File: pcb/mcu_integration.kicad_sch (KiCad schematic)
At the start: 26 parts, among them J1 Micro_SD_Card, J3 Conn_01x06, U1 STM32F103RBTx, Y1 ECS-80-18-5PX-GM-TR

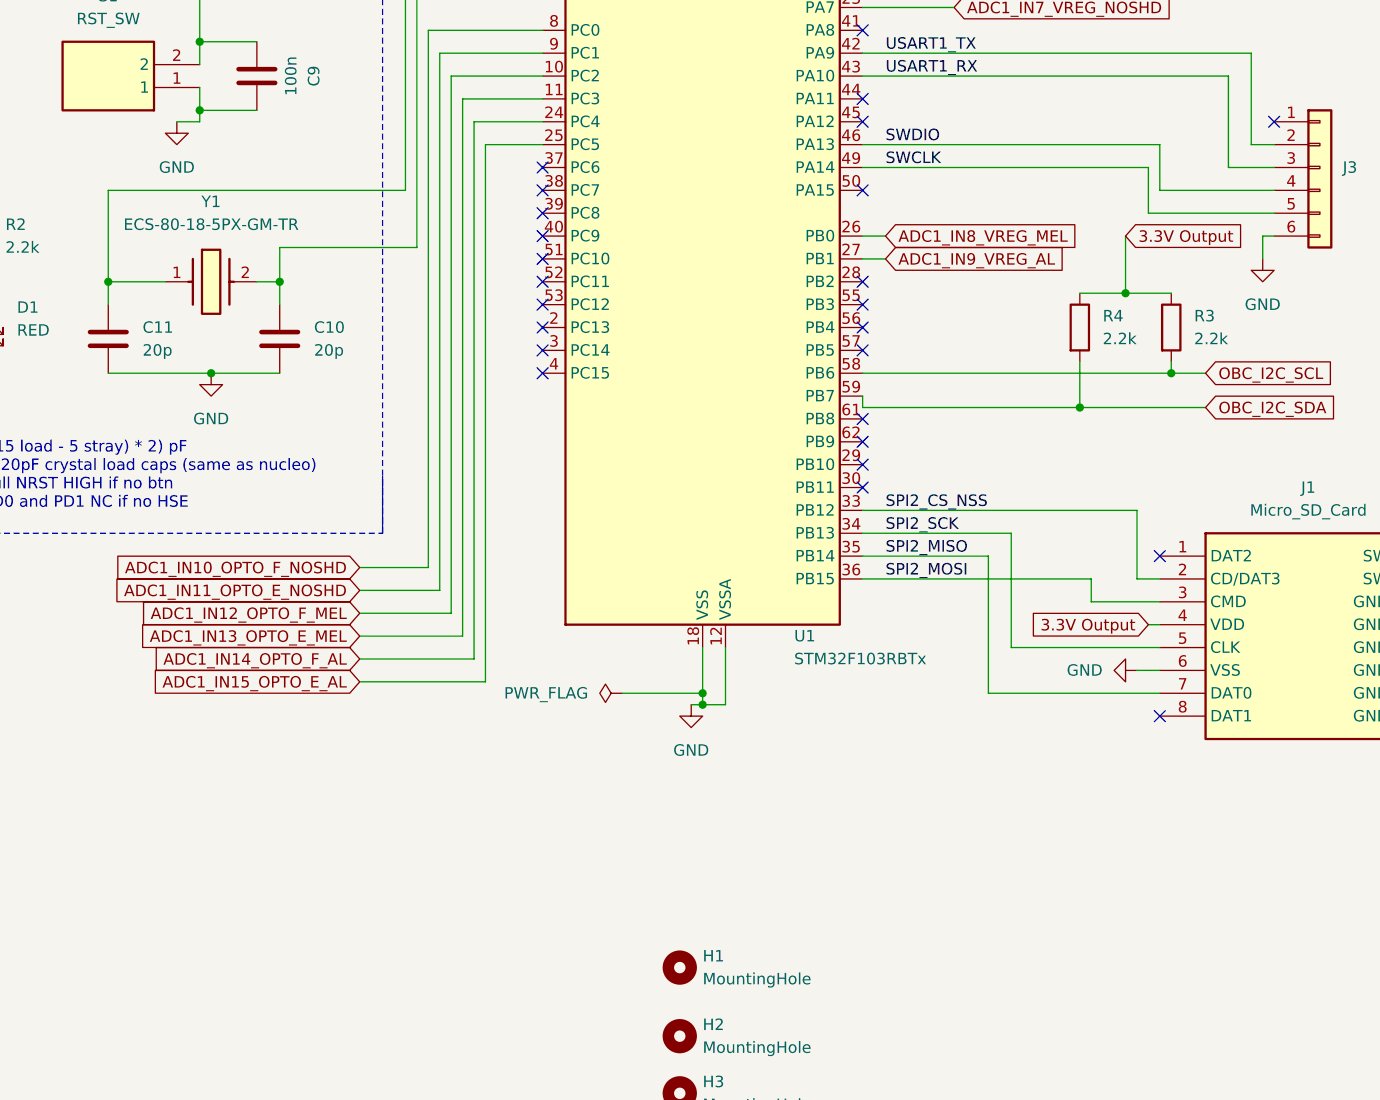
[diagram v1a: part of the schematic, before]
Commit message: Wire touchup, initial changes (#12)
* Implemented mosfet, decoupling

Please review functionality

* wire placement, inital revisions

made it more PCB ready with spacing and such
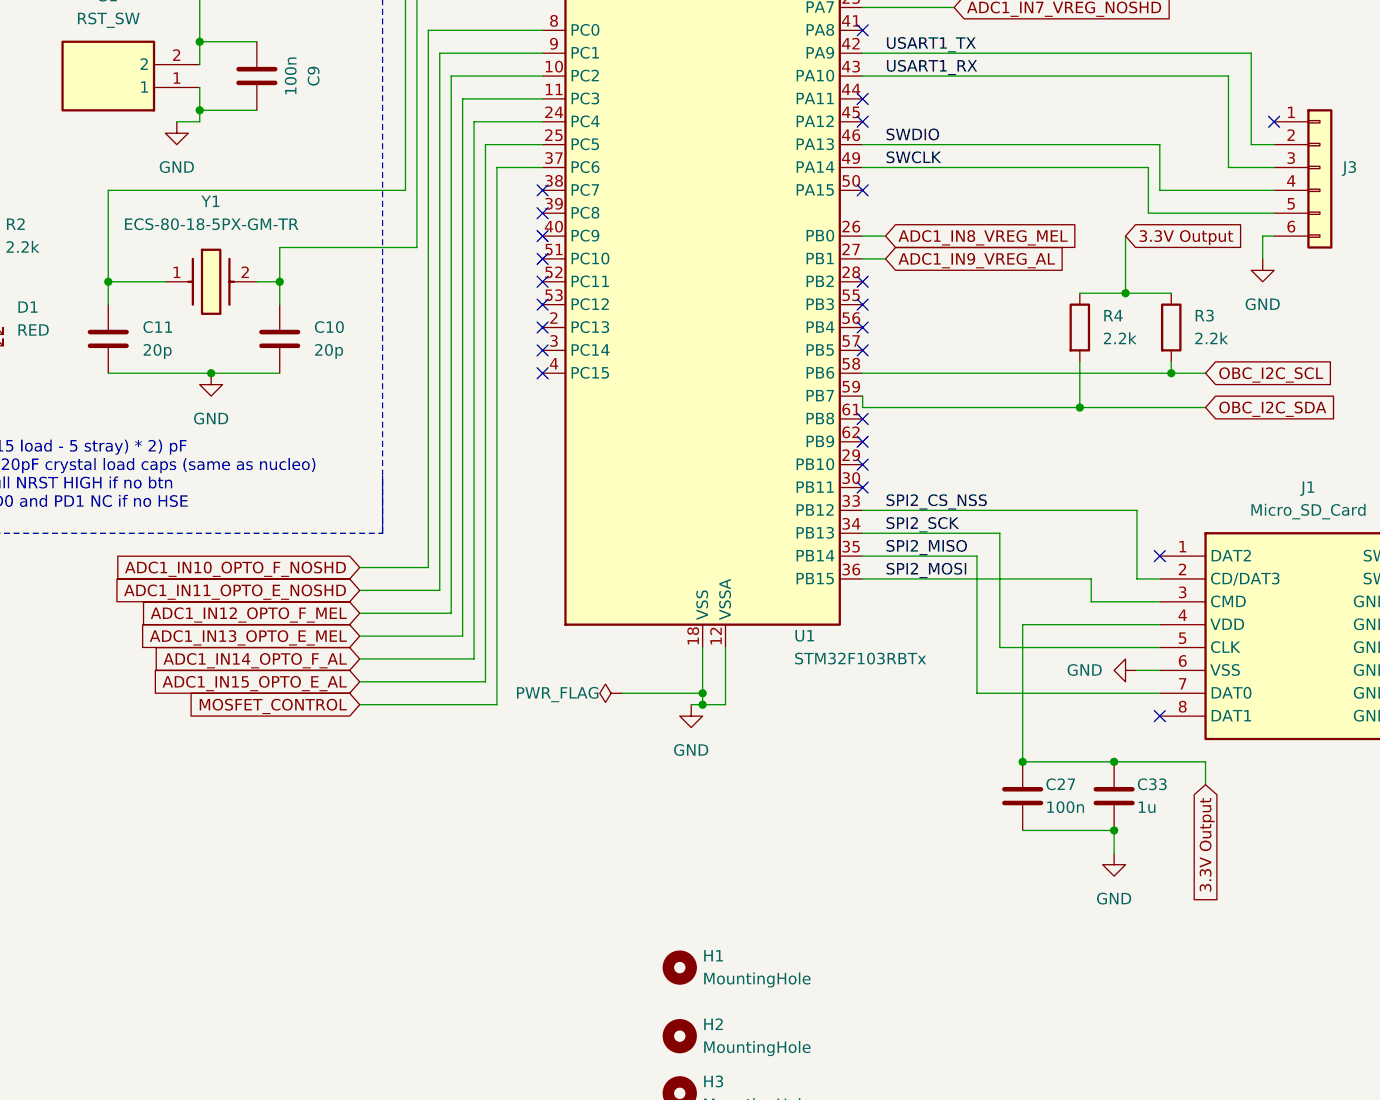
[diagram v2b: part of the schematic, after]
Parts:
- added C27: 100n, Capacitor_SMD:C_0402_1005Metric, symbol Device:C
- added C33: 1u, Capacitor_SMD:C_0402_1005Metric, symbol Device:C
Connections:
- net 3.3V Output: now also C27.1, C33.1
- net GND: now also C27.2, C33.2
- net MOSFET_CONTROL: now reaches U1.37 (PC6)
- no-connect marks 28 -> 27
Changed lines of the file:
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@@
   (junction (at 33.02 85.09) (diameter 0) (color 0 0 0 0)
   )
+  (junction (at 144.78 146.05) (diameter 0) (color 0 0 0 0)
+  )
   (junction (at 93.98 30.48) (diameter 0) (color 0 0 0 0)
   )
@@
   (junction (at 52.07 24.13) (diameter 0) (color 0 0 0 0)
   )
+  (junction (at 134.62 138.43) (diameter 0) (color 0 0 0 0)
+  )
   (junction (at 118.11 20.32) (diameter 0) (color 0 0 0 0)
   )
@@
   )
   (junction (at 63.5 24.13) (diameter 0) (color 0 0 0 0)
+  )
+  (junction (at 144.78 138.43) (diameter 0) (color 0 0 0 0)
   )
   (no_connect (at 81.28 90.17))
@@
   (no_connect (at 116.84 100.33))
   (no_connect (at 116.84 64.77))
-  (no_connect (at 81.28 72.39))
   (no_connect (at 182.88 118.11))
   (no_connect (at 116.84 74.93))
@@
   (no_connect (at 182.88 115.57))
   (no_connect (at 81.28 52.07))
+  (wire (pts (xy 134.62 146.05) (xy 144.78 146.05))
+    (stroke (width 0) (type default))
+  )
   (wire (pts (xy 39.37 24.13) (xy 52.07 24.13))
     (stroke (width 0) (type default))
@@
     (stroke (width 0) (type default))
   )
-  (wire (pts (xy 133.35 113.03) (xy 116.84 113.03))
+  (wire (pts (xy 132.08 113.03) (xy 116.84 113.03))
     (stroke (width 0) (type default))
   )
   (wire (pts (xy 66.04 46.99) (xy 81.28 46.99))
+    (stroke (width 0) (type default))
+  )
+  (wire (pts (xy 154.94 140.97) (xy 154.94 138.43))
     (stroke (width 0) (type default))
   )
@@
     (stroke (width 0) (type default))
   )
+  (wire (pts (xy 144.78 148.59) (xy 144.78 146.05))
+    (stroke (width 0) (type default))
+  )
+  (wire (pts (xy 60.96 132.08) (xy 76.2 132.08))
+    (stroke (width 0) (type default))
+  )
   (wire (pts (xy 106.68 21.59) (xy 106.68 31.75))
     (stroke (width 0) (type default))
@@
     (stroke (width 0) (type default))
   )
-  (wire (pts (xy 130.81 115.57) (xy 130.81 130.81))
+  (wire (pts (xy 129.54 115.57) (xy 129.54 130.81))
     (stroke (width 0) (type default))
   )
@@
     (stroke (width 0) (type default))
   )
-  (wire (pts (xy 149.86 125.73) (xy 133.35 125.73))
+  (wire (pts (xy 149.86 125.73) (xy 132.08 125.73))
     (stroke (width 0) (type default))
   )
@@
     (stroke (width 0) (type default))
   )
+  (wire (pts (xy 154.94 138.43) (xy 144.78 138.43))
+    (stroke (width 0) (type default))
+  )
   (wire (pts (xy 116.84 110.49) (xy 147.32 110.49))
     (stroke (width 0) (type default))
@@
   )
   (wire (pts (xy 146.05 80.01) (xy 146.05 86.36))
+    (stroke (width 0) (type default))
+  )
+  (wire (pts (xy 134.62 123.19) (xy 149.86 123.19))
     (stroke (width 0) (type default))
   )
@@
     (stroke (width 0) (type default))
   )
-  (wire (pts (xy 148.59 123.19) (xy 149.86 123.19))
-    (stroke (width 0) (type default))
-  )
   (wire (pts (xy 76.2 40.64) (xy 76.2 41.91))
     (stroke (width 0) (type default))
@@
     (stroke (width 0) (type default))
   )
+  (wire (pts (xy 129.54 130.81) (xy 149.86 130.81))
+    (stroke (width 0) (type default))
+  )
   (wire (pts (xy 52.07 81.28) (xy 67.31 81.28))
     (stroke (width 0) (type default))
   )
-  (wire (pts (xy 133.35 125.73) (xy 133.35 113.03))
+  (wire (pts (xy 132.08 125.73) (xy 132.08 113.03))
     (stroke (width 0) (type default))
   )
@@
     (stroke (width 0) (type dash))
   )
+  (wire (pts (xy 134.62 123.19) (xy 134.62 138.43))
+    (stroke (width 0) (type default))
+  )
   (wire (pts (xy 116.84 59.69) (xy 160.02 59.69))
     (stroke (width 0) (type default))
   )
-  (wire (pts (xy 130.81 130.81) (xy 149.86 130.81))
-    (stroke (width 0) (type default))
-  )
   (wire (pts (xy 147.32 110.49) (xy 147.32 118.11))
     (stroke (width 0) (type default))
   )
+  (wire (pts (xy 76.2 72.39) (xy 76.2 132.08))
+    (stroke (width 0) (type default))
+  )
   (wire (pts (xy 162.56 74.93) (xy 149.86 74.93))
     (stroke (width 0) (type default))
@@
     (stroke (width 0) (type default))
   )
+  (wire (pts (xy 134.62 138.43) (xy 144.78 138.43))
+    (stroke (width 0) (type default))
+  )
+  (wire (pts (xy 81.28 72.39) (xy 76.2 72.39))
+    (stroke (width 0) (type default))
+  )
   (wire (pts (xy 149.86 74.93) (xy 149.86 69.85))
     (stroke (width 0) (type default))
@@
     (stroke (width 0) (type default))
   )
-  (wire (pts (xy 116.84 115.57) (xy 130.81 115.57))
+  (wire (pts (xy 116.84 115.57) (xy 129.54 115.57))
     (stroke (width 0) (type default))
   )
@@
   (label "SPI2_SCK" (at 119.38 113.03 0) (fields_autoplaced)
     (effects (font (size 1.27 1.27)) (justify left bottom))
+  )
+  (global_label "3.3V Output" (shape input) (at 154.94 140.97 270) (fields_autoplaced)
+    (effects (font (size 1.27 1.27)) (justify right))
+    (property "Intersheetrefs" "${INTERSHEET_REFS}" (at 154.94 155.2641 90)
+      (effects (font (size 1.27 1.27)) (justify right) hide)
+    )
   )
   (global_label "ADC1_IN6_VREF_AL" (shape input) (at 127 52.07 0) (fields_autoplaced)
@@
     )
   )
+  (global_label "MOSFET_CONTROL" (shape input) (at 60.96 132.08 180) (fields_autoplaced)
+    (effects (font (size 1.27 1.27)) (justify right))
+    (property "Intersheetrefs" "${INTERSHEET_REFS}" (at 41.2834 132.08 0)
+      (effects (font (size 1.27 1.27)) (justify right) hide)
+    )
+  )
   (global_label "ADC1_IN2_OPAMP_MEL" (shape input) (at 127 41.91 0) (fields_autoplaced)
     (effects (font (size 1.27 1.27)) (justify left))
@@
     (property "Intersheetrefs" "${INTERSHEET_REFS}" (at 149.0956 49.53 0)
       (effects (font (size 1.27 1.27)) (justify left) hide)
-    )
-  )
-  (global_label "3.3V Output" (shape input) (at 148.59 123.19 180) (fields_autoplaced)
-    (effects (font (size 1.27 1.27)) (justify right))
-    (property "Intersheetrefs" "${INTERSHEET_REFS}" (at 134.2959 123.19 0)
-      (effects (font (size 1.27 1.27)) (justify right) hide)
     )
   )
@@
     )
   )
+  (symbol (lib_id "power:GND") (at 144.78 148.59 0) (unit 1)
+    (in_bom yes) (on_board yes) (dnp no) (fields_autoplaced)
+    (property "Reference" "#PWR05" (at 144.78 154.94 0)
+      (effects (font (size 1.27 1.27)) hide)
+    )
+    (property "Value" "GND" (at 144.78 153.67 0)
+      (effects (font (size 1.27 1.27)))
+    )
+    (property "Footprint" "" (at 144.78 148.59 0)
+      (effects (font (size 1.27 1.27)) hide)
+    )
+    (property "Datasheet" "" (at 144.78 148.59 0)
+      (effects (font (size 1.27 1.27)) hide)
+    )
+    (pin "1")
+    (instances
+      (project "mcu_integration"
+        (path "/c0210bc3-f67f-47d8-a34e-f002a728adb2"
+          (reference "#PWR05") (unit 1)
+        )
+      )
+    )
+  )
   (symbol (lib_id "Mechanical:MountingHole") (at 96.52 161.29 0) (unit 1)
     (in_bom yes) (on_board yes) (dnp no) (fields_autoplaced)
@@
   )
   (symbol (lib_id "power:GND") (at 147.32 128.27 270) (unit 1)
-    (in_bom yes) (on_board yes) (dnp no) (fields_autoplaced)
+    (in_bom yes) (on_board yes) (dnp no)
     (property "Reference" "#PWR023" (at 140.97 128.27 0)
       (effects (font (size 1.27 1.27)) hide)
@@
     )
   )
+  (symbol (lib_id "Device:C") (at 134.62 142.24 0) (unit 1)
+    (in_bom yes) (on_board yes) (dnp no)
+    (property "Reference" "C27" (at 137.16 140.97 0)
+      (effects (font (size 1.27 1.27)) (justify left))
+    )
+    (property "Value" "100n" (at 137.16 143.51 0)
+      (effects (font (size 1.27 1.27)) (justify left))
+    )
+    (property "Footprint" "Capacitor_SMD:C_0402_1005Metric" (at 135.5852 146.05 0)
+      (effects (font (size 1.27 1.27)) hide)
+    )
+    (property "Datasheet" "~" (at 134.62 142.24 0)
+      (effects (font (size 1.27 1.27)) hide)
+    )
+    (pin "1")
+    (pin "2")
+    (instances
+      (project "mcu_integration"
+        (path "/c0210bc3-f67f-47d8-a34e-f002a728adb2"
+          (reference "C27") (unit 1)
+        )
+      )
+    )
+  )
   (symbol (lib_id "power:GND") (at 19.05 91.44 0) (unit 1)
     (in_bom yes) (on_board yes) (dnp no) (fields_autoplaced)
@@
         (path "/c0210bc3-f67f-47d8-a34e-f002a728adb2"
           (reference "C7") (unit 1)
+        )
+      )
+    )
+  )
+  (symbol (lib_id "Device:C") (at 144.78 142.24 0) (unit 1)
+    (in_bom yes) (on_board yes) (dnp no)
+    (property "Reference" "C33" (at 147.32 140.97 0)
+      (effects (font (size 1.27 1.27)) (justify left))
+    )
+    (property "Value" "1u" (at 147.32 143.51 0)
+      (effects (font (size 1.27 1.27)) (justify left))
+    )
+    (property "Footprint" "Capacitor_SMD:C_0402_1005Metric" (at 145.7452 146.05 0)
+      (effects (font (size 1.27 1.27)) hide)
+    )
+    (property "Datasheet" "~" (at 144.78 142.24 0)
+      (effects (font (size 1.27 1.27)) hide)
+    )
+    (pin "1")
+    (pin "2")
+    (instances
+      (project "mcu_integration"
+        (path "/c0210bc3-f67f-47d8-a34e-f002a728adb2"
+          (reference "C33") (unit 1)
         )
       )
@@
   )
   (symbol (lib_id "power:PWR_FLAG") (at 90.17 130.81 90) (unit 1)
-    (in_bom yes) (on_board yes) (dnp no) (fields_autoplaced)
+    (in_bom yes) (on_board yes) (dnp no)
     (property "Reference" "#FLG03" (at 88.265 130.81 0)
       (effects (font (size 1.27 1.27)) hide)
     )
-    (property "Value" "PWR_FLAG" (at 86.36 130.81 90)
-      (effects (font (size 1.27 1.27)) (justify left))
-    )
+    (property "Value" "PWR_FLAG" (at 87.63 130.81 90)
+      (effects (font (size 1.27 1.27)) (justify left))
+    )

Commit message: done layout/ratsnet
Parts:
- J1: footprint (none) -> capstone:22017781
- J3: footprint Connector_PinHeader_2.54mm:PinHeader_1x06_P2.54mm_Horizontal -> Connector_PinHeader_2.54mm:PinHeader_1x06_P2.54mm_Vertical
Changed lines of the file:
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@@
       (effects (font (size 1.27 1.27)) (justify left) hide)
     )
-    (property "Footprint" "Connector_PinHeader_2.54mm:PinHeader_1x06_P2.54mm_Horizontal" (at 167.64 72.39 0)
+    (property "Footprint" "Connector_PinHeader_2.54mm:PinHeader_1x06_P2.54mm_Vertical" (at 167.64 72.39 0)
       (effects (font (size 1.27 1.27)) hide)
     )
@@
       (effects (font (size 1.27 1.27)))
     )
-    (property "Footprint" "" (at 179.07 210.49 0)
-      (effects (font (size 1.27 1.27)) (justify left top) hide)
-    )
+    (property "Footprint" "capstone:22017781" (at 179.07 210.49 0)
+      (effects (font (size 1.27 1.27)) (justify left top) hide)
+    )

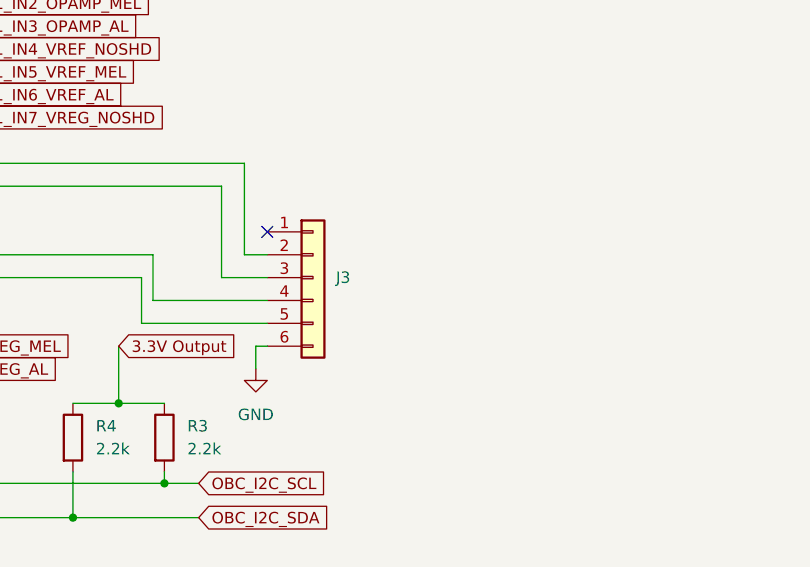
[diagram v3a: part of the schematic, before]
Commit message: fixed all errors and warnings, silk fixed
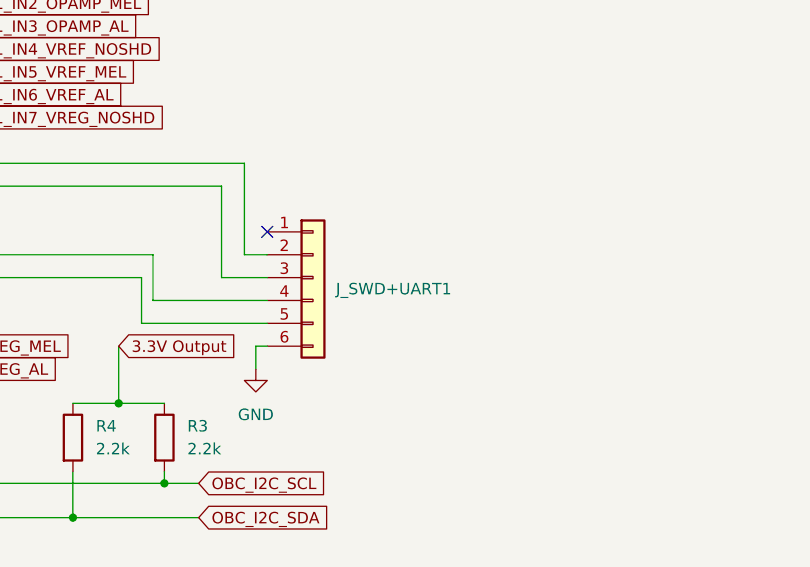
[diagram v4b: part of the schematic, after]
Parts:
- renumbered J3 to J_SWD+UART1
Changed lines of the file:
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@@
   (symbol (lib_id "Connector_Generic:Conn_01x06") (at 167.64 72.39 0) (unit 1)
     (in_bom yes) (on_board yes) (dnp no) (fields_autoplaced)
-    (property "Reference" "J3" (at 170.18 72.39 0)
+    (property "Reference" "J_SWD+UART1" (at 170.18 73.66 0)
       (effects (font (size 1.27 1.27)) (justify left))
     )
@@
       (project "mcu_integration"
         (path "/c0210bc3-f67f-47d8-a34e-f002a728adb2"
-          (reference "J3") (unit 1)
+          (reference "J_SWD+UART1") (unit 1)
         )
       )

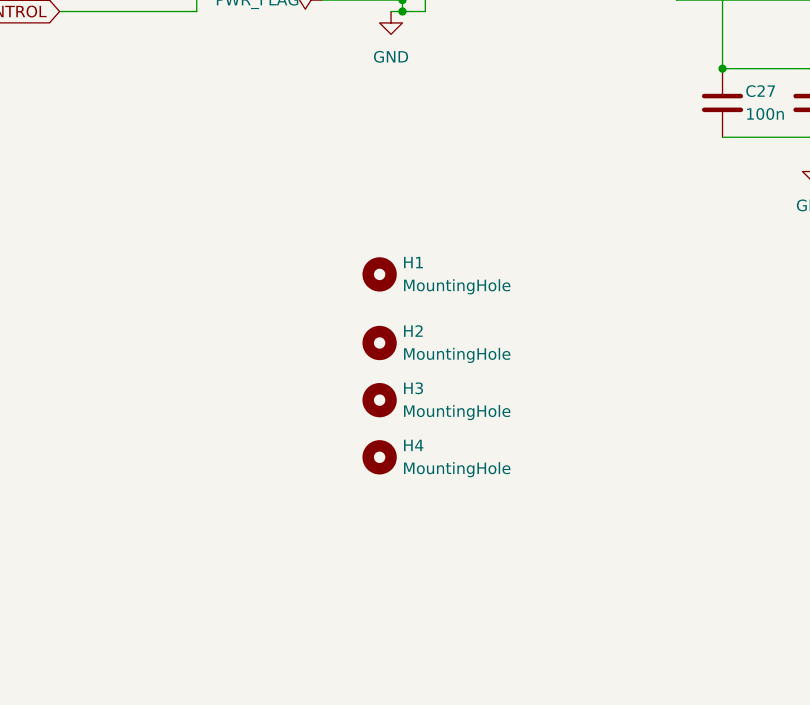
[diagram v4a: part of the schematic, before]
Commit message: proper holes added
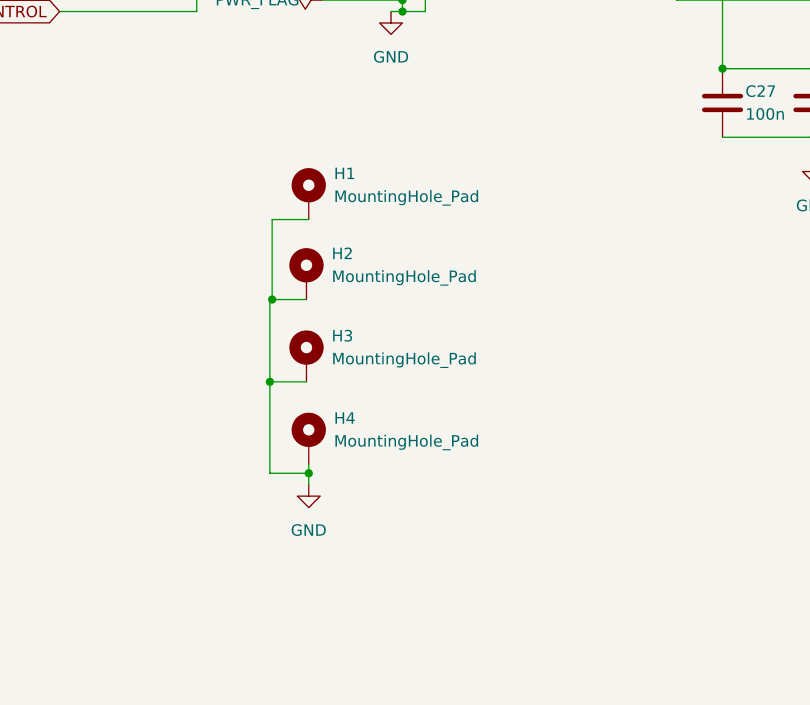
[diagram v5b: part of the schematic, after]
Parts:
- removed H1, H2, H3, H4: MountingHole, MountingHole:MountingHole_2.2mm_M2, symbol Mechanical:MountingHole
- added H1, H2, H3, H4: MountingHole_Pad, MountingHole:MountingHole_3.2mm_M3_Pad_Via, symbol Mechanical:MountingHole_Pad
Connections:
- net GND: now also H1.1, H2.1, H3.1, H4.1
